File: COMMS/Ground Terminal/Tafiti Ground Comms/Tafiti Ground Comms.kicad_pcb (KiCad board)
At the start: 4 copper layers, 64.5 x 73.6 mm, 64 parts, among them J1 USB_B_Micro, J2 USB_B_Micro, J3 Micro_SD_Card_Det, J4 Conn_01x08_Male, SW1 SW_SPDT, SW2 SW_Push, U1 STM32H743VIT6, U2 AMS1117-3.3, U3 Ai-Thinker-Ra-02, U4 Ai-Thinker-Ra-02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

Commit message: Finished the PCB layout
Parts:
- moved D3 9.35 mm to (101.2, 149.7)
- moved J2 6.19 mm to (108.8, 151.7)
- moved D1 3.67 mm to (124.8, 142.0)
- moved R1 3.67 mm to (124.8, 139.2)
- moved C8 2.61 mm to (134.9, 121.0)
- moved D6 2.56 mm to (111.3, 136.4)
- moved 1k1 2.10 mm to (118.9, 145.5)
- moved D5 2.10 mm to (105.5, 145.5)
- moved D7 2.10 mm to (118.1, 140.7)
- moved D8 2.10 mm to (118.1, 142.5)
- moved R11 2.10 mm to (115.6, 147.2)
- moved R12 2.10 mm to (115.6, 150.5)
- moved R13 2.10 mm to (115.1, 140.9)
- moved R14 2.10 mm to (115.1, 142.2)
- moved U5 2.10 mm to (110.9, 141.3)
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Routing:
- net VBUS: track 0.00 -> 118.6 mm, vias 0 -> 5
- net GND: track 0.00 -> 94.9 mm, vias 0 -> 43
- net +3V3: track 0.00 -> 76.1 mm, vias 0 -> 22
- net SDMMC_DA: track 0.00 -> 69.5 mm, vias 0 -> 2
- net SDMMC_DB: track 0.00 -> 51.3 mm, vias 0 -> 2
- net IRQ1: track 0.00 -> 49.0 mm
- net ExtTRIG: track 0.00 -> 42.7 mm, vias 0 -> 2
- net RESET: track 0.00 -> 42.1 mm, vias 0 -> 2
- net SWDIO: track 0.00 -> 41.9 mm
- net USB_D+: track 0.00 -> 39.0 mm, vias 0 -> 2
- net USB_DM+: track 0.00 -> 37.1 mm
- net USB_D-: track 0.00 -> 36.5 mm, vias 0 -> 2
- net SDMMC_D0: track 0.00 -> 36.3 mm, vias 0 -> 2
- net USB_DM-: track 0.00 -> 35.8 mm
- net SWO: track 0.00 -> 35.4 mm, vias 0 -> 1
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- added copper zone on F.Cu, net +3V3
- added copper zone on In2.Cu, net +3V3
- added copper zone on F.Cu, net GND
- added copper zone on In1.Cu, net GND
- added copper zone on F.Cu, net VBUS

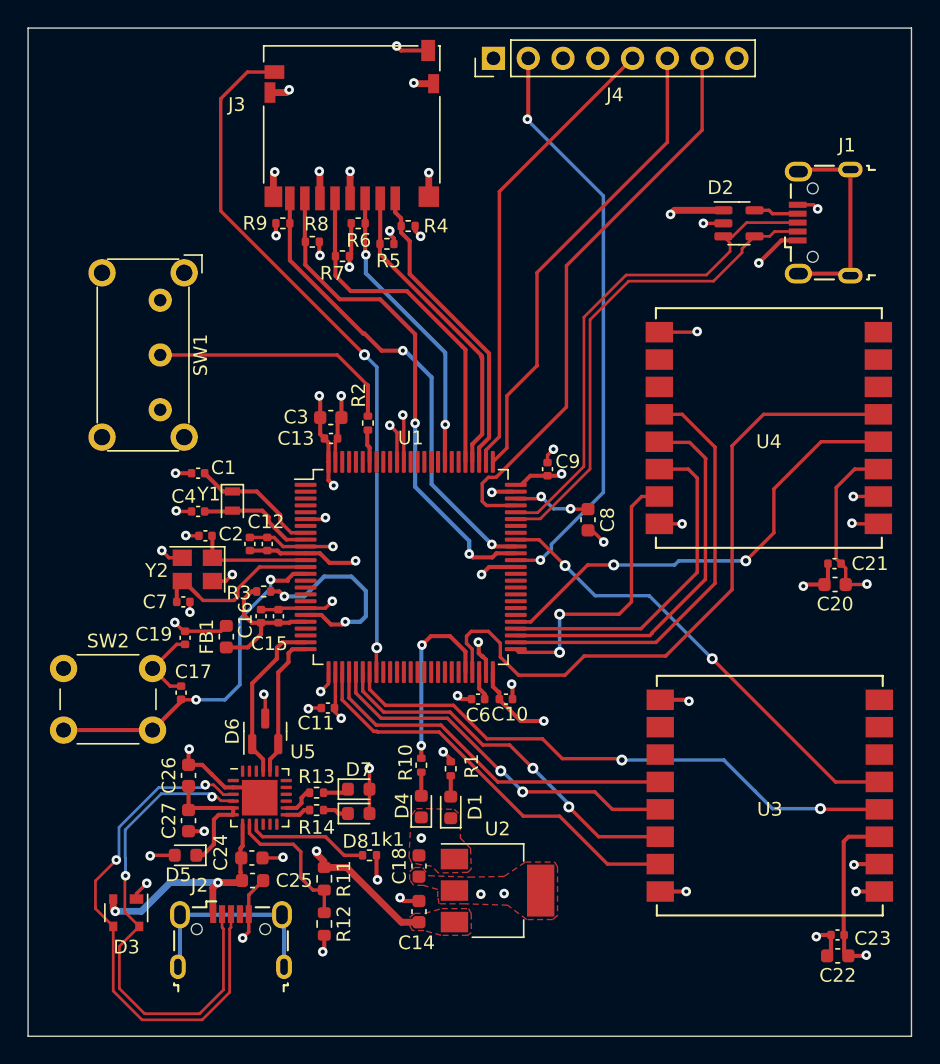
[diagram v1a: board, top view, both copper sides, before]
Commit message: Added the models for the USB and Lora Modules as well as the Silkscreen
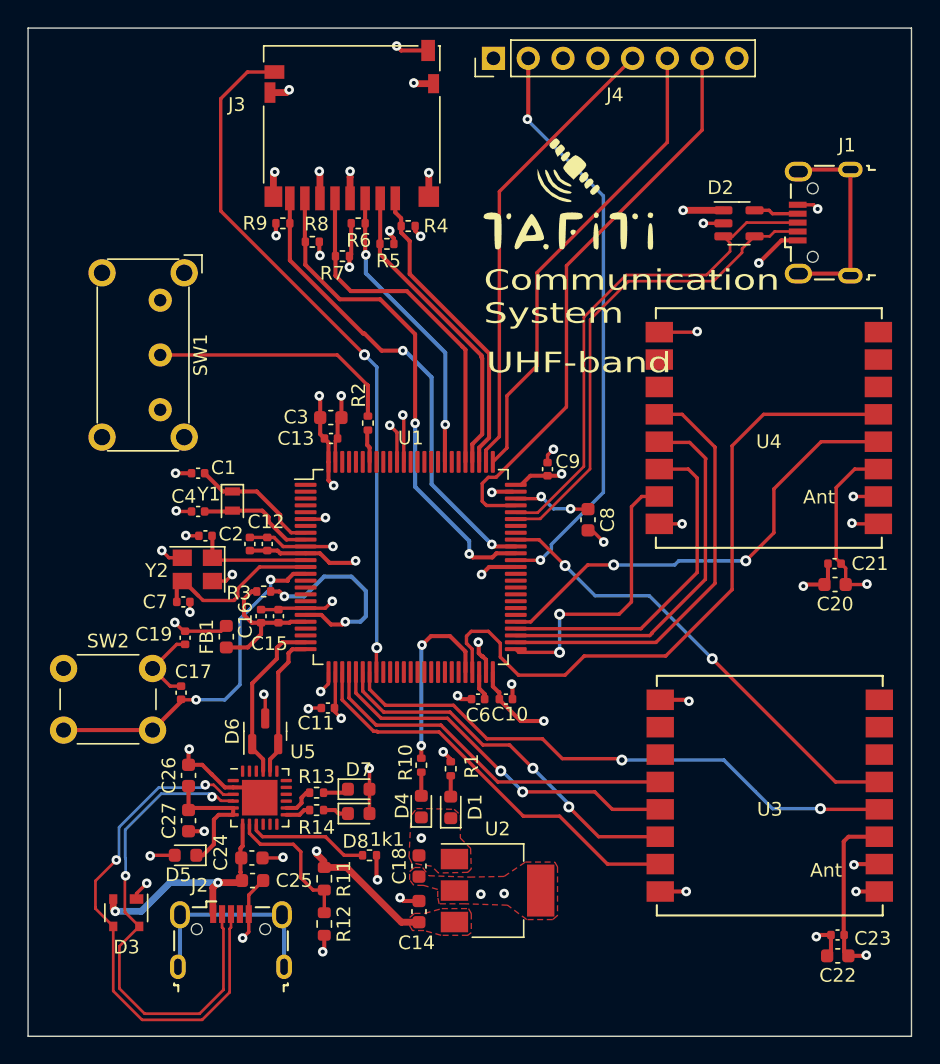
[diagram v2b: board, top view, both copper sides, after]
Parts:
- added G***: LOGO, LOGO, F.Cu at (133.8, 97.6)
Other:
- board text added: "Ant"
- board text added: "Communication Subsystem"
- board text added: "Communication System"
- board text added: "Kenya Space Agency"
- board text added: "Tafiti Nano-satellite"
- board text added: "UHF-band"
- board text added: "V1.3"
